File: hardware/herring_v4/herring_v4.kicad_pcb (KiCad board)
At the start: 2 copper layers, 7 parts, among them U1 W65C02, U2 AS6C62256, U3 ATF16V8B, U4 AT28C64B, U5 W65C51, X1 CXO_DIP14, X2 CXO_DIP8

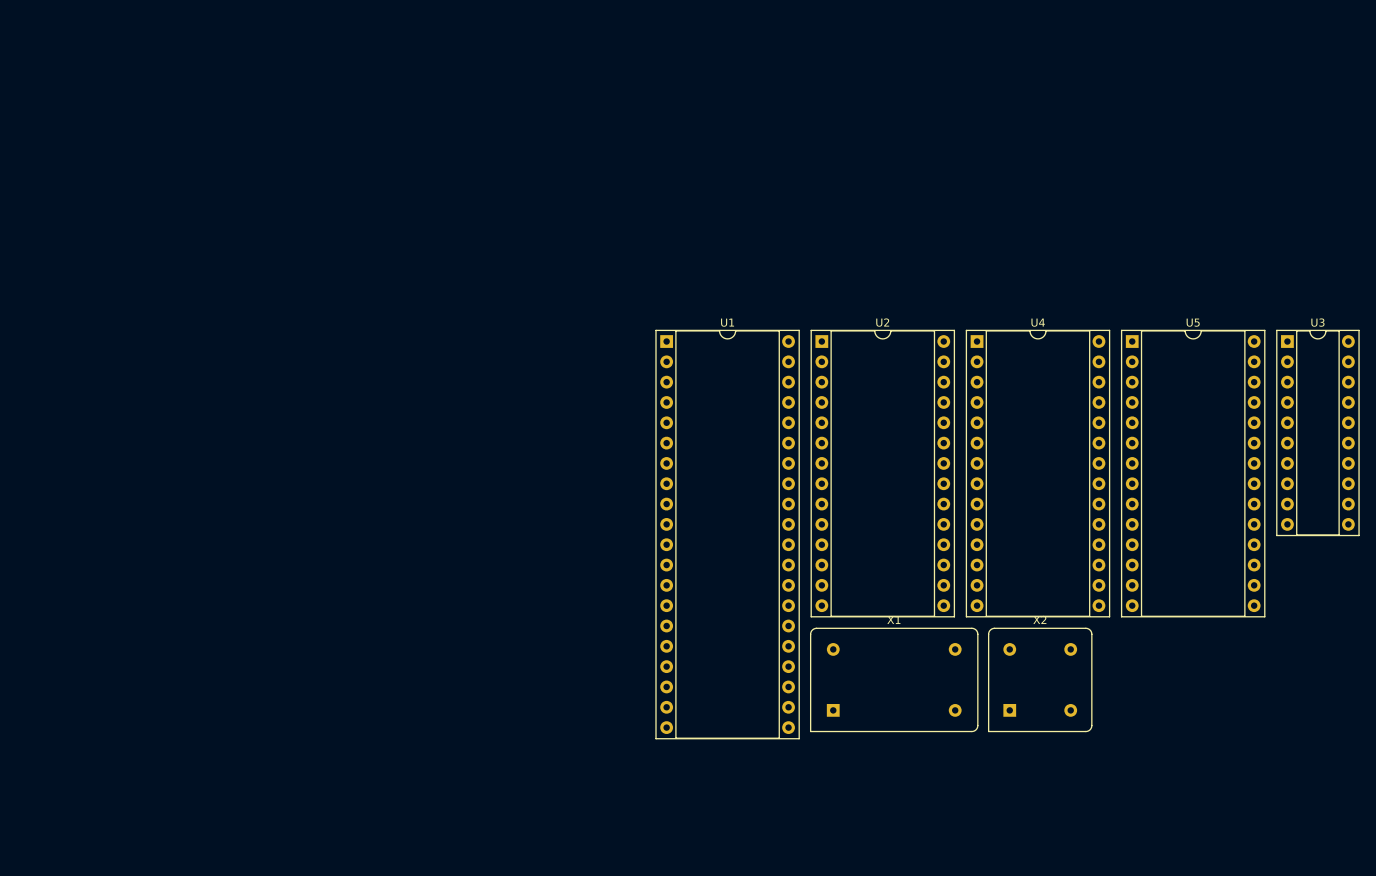
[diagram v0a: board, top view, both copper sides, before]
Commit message: Add 16C550 to schematic
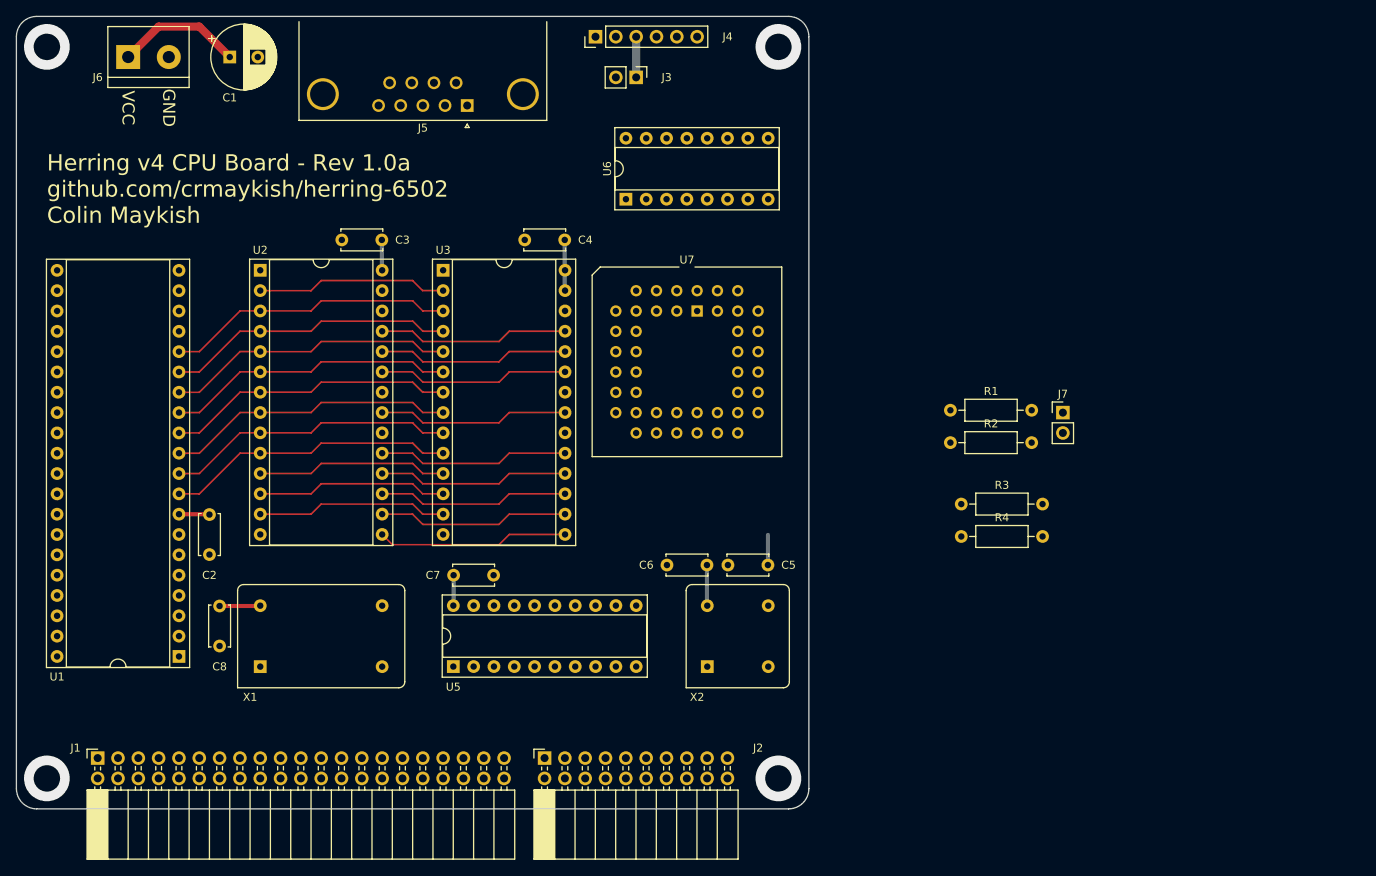
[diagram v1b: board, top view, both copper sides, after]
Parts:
- removed the U5 at (164.9, 66.0)
- added C1: 100uF, Capacitor_THT:CP_Radial_D8.0mm_P3.50mm, F.Cu at (52.1, 30.5)
- added C2: 0.1uF, Capacitor_THT:C_Disc_D5.0mm_W2.5mm_P5.00mm, F.Cu at (49.5, 87.7)
- added C3: 0.1uF, Capacitor_THT:C_Disc_D5.0mm_W2.5mm_P5.00mm, F.Cu at (71.1, 53.3)
- added C4: 0.1uF, Capacitor_THT:C_Disc_D5.0mm_W2.5mm_P5.00mm, F.Cu at (93.9, 53.3)
- added C5: 0.1uF, Capacitor_THT:C_Disc_D5.0mm_W2.5mm_P5.00mm, F.Cu at (119.3, 94.0)
- added C6: 0.1uF, Capacitor_THT:C_Disc_D5.0mm_W2.5mm_P5.00mm, F.Cu at (111.7, 94.0)
- added C7: 0.1uF, Capacitor_THT:C_Disc_D5.0mm_W2.5mm_P5.00mm, F.Cu at (80.0, 95.2)
- added C8: 0.1uF, Capacitor_THT:C_Disc_D5.0mm_W2.5mm_P5.00mm, F.Cu at (50.8, 99.1)
- added J1: Conn_02x20_Odd_Even, Connector_PinSocket_2.54mm:PinSocket_2x21_P2.54mm_Horizontal, F.Cu at (35.6, 118.1)
- added J2: Conn_02x10_Odd_Even, Connector_PinSocket_2.54mm:PinSocket_2x10_P2.54mm_Horizontal, F.Cu at (91.4, 118.1)
- added J3: Conn_01x02_Male, Connector_PinHeader_2.54mm:PinHeader_1x02_P2.54mm_Vertical, F.Cu at (102.9, 33.0)
- added J4: Conn_01x06_Male, Connector_PinHeader_2.54mm:PinHeader_1x06_P2.54mm_Vertical, F.Cu at (97.8, 27.9)
- added J5: DB9_Male_MountingHoles, Connector_Dsub:DSUB-9_Male_Horizontal_P2.77x2.84mm_EdgePinOffset7.70mm_Housed_MountingHolesOffset9.12mm, F.Cu at (81.8, 36.5)
- added J6: Screw_Terminal_01x02, TerminalBlock:TerminalBlock_bornier-2_P5.08mm, F.Cu at (39.4, 30.5)
- added J7: Conn_01x02_Male, Connector_PinHeader_2.54mm:PinHeader_1x02_P2.54mm_Vertical, F.Cu at (156.2, 74.9)
- added R1: 4k7, Resistor_THT:R_Axial_DIN0207_L6.3mm_D2.5mm_P10.16mm_Horizontal, F.Cu at (142.2, 74.6)
- added R2: 4k7, Resistor_THT:R_Axial_DIN0207_L6.3mm_D2.5mm_P10.16mm_Horizontal, F.Cu at (142.2, 78.7)
- added R3: 4k7, Resistor_THT:R_Axial_DIN0207_L6.3mm_D2.5mm_P10.16mm_Horizontal, F.Cu at (143.5, 86.4)
- added R4: 4k7, Resistor_THT:R_Axial_DIN0207_L6.3mm_D2.5mm_P10.16mm_Horizontal, F.Cu at (143.5, 90.4)
- added U6: MAX3232, Package_DIP:DIP-16_W7.62mm_Socket, F.Cu at (101.6, 48.2)
- added U7: 16C550, Package_LCC:PLCC-44_THT-Socket, F.Cu at (110.5, 62.2)
- moved U5 111.9 mm to (80.0, 106.7), turned to 90 degrees
- moved U1 72.6 mm to (45.7, 105.4), turned to 180 degrees
- moved X1 71.8 mm to (55.9, 106.7)
- moved U2 70.8 mm to (55.9, 57.1)
- moved U3 67.3 mm to (78.7, 57.1)
- moved X2 38.2 mm to (111.8, 106.7)
- renumbered U4 to U3, U3 to U5
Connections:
- U1 pad 10: unconnected-(U1-Pad10) -> /A1
- U1 pad 11: unconnected-(U1-Pad11) -> /A2
- U1 pad 12: unconnected-(U1-Pad12) -> /A3
- U1 pad 13: unconnected-(U1-Pad13) -> /A4
- U1 pad 14: unconnected-(U1-Pad14) -> /A5
- U1 pad 15: unconnected-(U1-Pad15) -> /A6
- U1 pad 16: unconnected-(U1-Pad16) -> /A7
- U1 pad 17: unconnected-(U1-Pad17) -> /A8
- U1 pad 18: unconnected-(U1-Pad18) -> /A9
- U1 pad 19: unconnected-(U1-Pad19) -> /A10
- U1 pad 2: unconnected-(U1-Pad2) -> /~{WAIT}
- U1 pad 20: unconnected-(U1-Pad20) -> /A11
- U1 pad 22: (no net) -> /A12
- U1 pad 23: unconnected-(U1-Pad23) -> /A13
- U1 pad 24: unconnected-(U1-Pad24) -> /A14
- U1 pad 25: unconnected-(U1-Pad25) -> /A15
- U1 pad 26: unconnected-(U1-Pad26) -> /D7
- U1 pad 27: unconnected-(U1-Pad27) -> /D6
- U1 pad 28: unconnected-(U1-Pad28) -> /D5
- U1 pad 29: unconnected-(U1-Pad29) -> /D4
- U1 pad 30: unconnected-(U1-Pad30) -> /D3
- U1 pad 31: unconnected-(U1-Pad31) -> /D2
- U1 pad 32: unconnected-(U1-Pad32) -> /D1
- U1 pad 33: unconnected-(U1-Pad33) -> /D0
- U1 pad 34: unconnected-(U1-Pad34) -> /~{RD}
- U1 pad 36: unconnected-(U1-Pad36) -> /~{BUSREQ}
- U1 pad 37: unconnected-(U1-Pad37) -> /PHI
- U1 pad 38: unconnected-(U1-Pad38) -> VCC
- U1 pad 4: unconnected-(U1-Pad4) -> /~{INT}
- U1 pad 40: unconnected-(U1-Pad40) -> /~{RESOUT}
- U1 pad 6: unconnected-(U1-Pad6) -> /~{NMI}
- U1 pad 9: unconnected-(U1-Pad9) -> /A0
- U2 pad 1: unconnected-(U2-Pad1) -> /A14
- U2 pad 10: unconnected-(U2-Pad10) -> /A0
- U2 pad 11: unconnected-(U2-Pad11) -> /D0
- U2 pad 12: unconnected-(U2-Pad12) -> /D1
- U2 pad 13: unconnected-(U2-Pad13) -> /D2
- U2 pad 15: unconnected-(U2-Pad15) -> /D3
- U2 pad 16: unconnected-(U2-Pad16) -> /D4
- U2 pad 17: unconnected-(U2-Pad17) -> /D5
- U2 pad 18: unconnected-(U2-Pad18) -> /D6
- U2 pad 19: unconnected-(U2-Pad19) -> /D7
- U2 pad 2: unconnected-(U2-Pad2) -> /A12
- U2 pad 20: unconnected-(U2-Pad20) -> /~{CSRAM}
- U2 pad 21: unconnected-(U2-Pad21) -> /A10
- U2 pad 22: unconnected-(U2-Pad22) -> GND
- U2 pad 23: unconnected-(U2-Pad23) -> /A11
- U2 pad 24: unconnected-(U2-Pad24) -> /A9
- U2 pad 25: unconnected-(U2-Pad25) -> /A8
- U2 pad 26: unconnected-(U2-Pad26) -> /A13
- U2 pad 27: unconnected-(U2-Pad27) -> /~{MEMWR}
- U2 pad 3: unconnected-(U2-Pad3) -> /A7
- U2 pad 4: unconnected-(U2-Pad4) -> /A6
- U2 pad 5: unconnected-(U2-Pad5) -> /A5
- U2 pad 6: unconnected-(U2-Pad6) -> /A4
- U2 pad 7: unconnected-(U2-Pad7) -> /A3
- U2 pad 8: unconnected-(U2-Pad8) -> /A2
- U2 pad 9: unconnected-(U2-Pad9) -> /A1
- U3 pad 10: unconnected-(U4-Pad10) -> /A0
- U3 pad 11: unconnected-(U4-Pad11) -> /D0
- U3 pad 12: unconnected-(U4-Pad12) -> /D1
- U3 pad 13: unconnected-(U4-Pad13) -> /D2
- U3 pad 15: unconnected-(U4-Pad15) -> /D3
- U3 pad 16: unconnected-(U4-Pad16) -> /D4
- U3 pad 17: unconnected-(U4-Pad17) -> /D5
- U3 pad 18: unconnected-(U4-Pad18) -> /D6
- U3 pad 19: unconnected-(U4-Pad19) -> /D7
- U3 pad 2: unconnected-(U4-Pad2) -> /A12
- U3 pad 20: unconnected-(U4-Pad20) -> /~{CSROM}
- U3 pad 21: unconnected-(U4-Pad21) -> /A10
- U3 pad 22: unconnected-(U4-Pad22) -> GND
- U3 pad 23: unconnected-(U4-Pad23) -> /A11
- U3 pad 24: unconnected-(U4-Pad24) -> /A9
- U3 pad 25: unconnected-(U4-Pad25) -> /A8
- U3 pad 27: unconnected-(U4-Pad27) -> VCC
- U3 pad 3: unconnected-(U4-Pad3) -> /A7
- U3 pad 4: unconnected-(U4-Pad4) -> /A6
- U3 pad 5: unconnected-(U4-Pad5) -> /A5
- U3 pad 6: unconnected-(U4-Pad6) -> /A4
- U3 pad 7: unconnected-(U4-Pad7) -> /A3
- U3 pad 8: unconnected-(U4-Pad8) -> /A2
- U3 pad 9: unconnected-(U4-Pad9) -> /A1
- U5 pad 1: unconnected-(U3-Pad1) (its old number) -> /PHI
- U5 pad 12: unconnected-(U3-Pad12) -> /~{MEMREQ}
- U5 pad 13: unconnected-(U3-Pad13) -> /~{RD}
- U5 pad 14: unconnected-(U3-Pad14) -> /~{WR}
- U5 pad 15: unconnected-(U3-Pad15) -> /~{IOREQ}
- U5 pad 16: unconnected-(U3-Pad16) -> /~{CSACIA}
- U5 pad 17: unconnected-(U3-Pad17) -> /~{CSROM}
- U5 pad 18: unconnected-(U3-Pad18) -> /~{CSRAM}
- U5 pad 19: unconnected-(U3-Pad19) -> /~{MEMWR}
- U5 pad 2: unconnected-(U3-Pad2) -> /A8
- U5 pad 3: unconnected-(U3-Pad3) -> /A9
- U5 pad 4: unconnected-(U3-Pad4) -> /A10
- U5 pad 5: unconnected-(U3-Pad5) -> /A11
- U5 pad 6: unconnected-(U3-Pad6) -> /A12
- U5 pad 7: unconnected-(U3-Pad7) -> /A13
- U5 pad 8: unconnected-(U3-Pad8) -> /A14
- U5 pad 9: unconnected-(U3-Pad9) -> /A15
- X1 pad 8: unconnected-(X1-Pad8) -> /PHI
- X2 pad 5: unconnected-(X2-Pad5) -> Net-(U4-Pad6)
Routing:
- net VCC: track 0.00 -> 47.7 mm
- net /A5: track 0.00 -> 36.2 mm
- net /A0: track 0.00 -> 36.2 mm
- net /A1: track 0.00 -> 36.2 mm
- net /A4: track 0.00 -> 36.2 mm
- net /A3: track 0.00 -> 36.2 mm
- net /A7: track 0.00 -> 36.2 mm
- net /A2: track 0.00 -> 36.2 mm
- net /A6: track 0.00 -> 36.2 mm
- net /D3: track 0.00 -> 23.9 mm
- net /D4: track 0.00 -> 23.9 mm
- net /A8: track 0.00 -> 23.9 mm
- net /A11: track 0.00 -> 23.9 mm
- net /A10: track 0.00 -> 23.9 mm
- net /D7: track 0.00 -> 23.9 mm
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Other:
- board outline added: 99.1 x 99.1 mm
- board text added: "GND"
- board text added: "Herring v4 CPU Board - Rev 1.0a github.com/crmaykish/herring-6502 Colin Maykish"
- board text added: "VCC"

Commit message: Strip down CPU board schematic
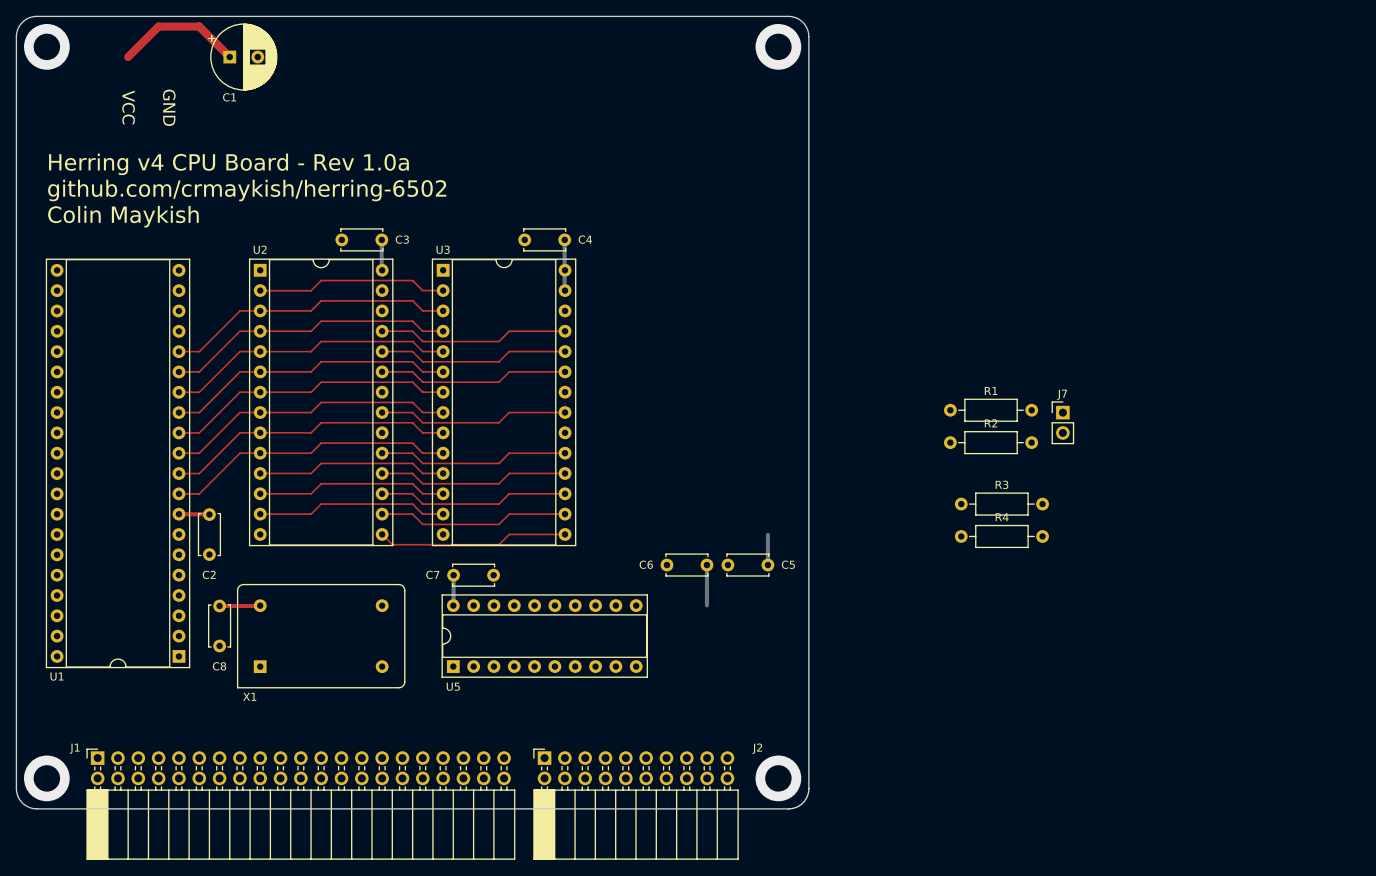
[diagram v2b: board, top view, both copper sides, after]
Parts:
- removed J3: Conn_01x02_Male, Connector_PinHeader_2.54mm:PinHeader_1x02_P2.54mm_Vertical
- removed J4: Conn_01x06_Male, Connector_PinHeader_2.54mm:PinHeader_1x06_P2.54mm_Vertical
- removed J5: DB9_Male_MountingHoles, Connector_Dsub:DSUB-9_Male_Horizontal_P2.77x2.84mm_EdgePinOffset7.70mm_Housed_MountingHolesOffset9.12mm
- removed J6: Screw_Terminal_01x02, TerminalBlock:TerminalBlock_bornier-2_P5.08mm
- removed U6: MAX3232, Package_DIP:DIP-16_W7.62mm_Socket
- removed U7: 16C550, Package_LCC:PLCC-44_THT-Socket
- removed X2: CXO_DIP8, Oscillator:Oscillator_DIP-8
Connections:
- J1 pad 37: /~{RD} -> unconnected-(J1-Pad37)
- J1 pad 38: /~{WR} -> unconnected-(J1-Pad38)
- U5 pad 16: /~{CSACIA} -> unconnected-(U5-Pad16)
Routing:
- net Net-(J3-Pad1): track 5.08 -> 0.00 mm
